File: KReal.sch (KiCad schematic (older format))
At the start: 30 parts, among them J101 USB, J102 3mm, J103 3mm, J104 3mm, J105 3mm, P101 X AXIS, P102 Y AXIS, P103 Z AXIS, P104 A AXIS, P105 X SW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

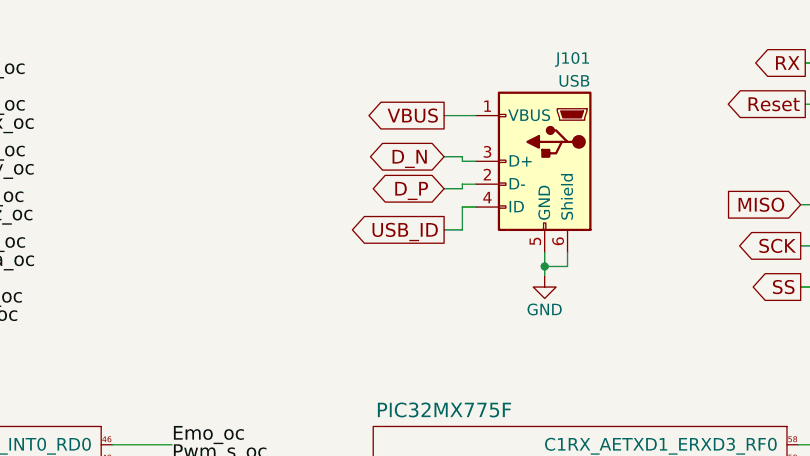
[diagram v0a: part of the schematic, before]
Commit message: Fixed swapped USB N and P lanes in schematic. NOT fixed in layout yet.
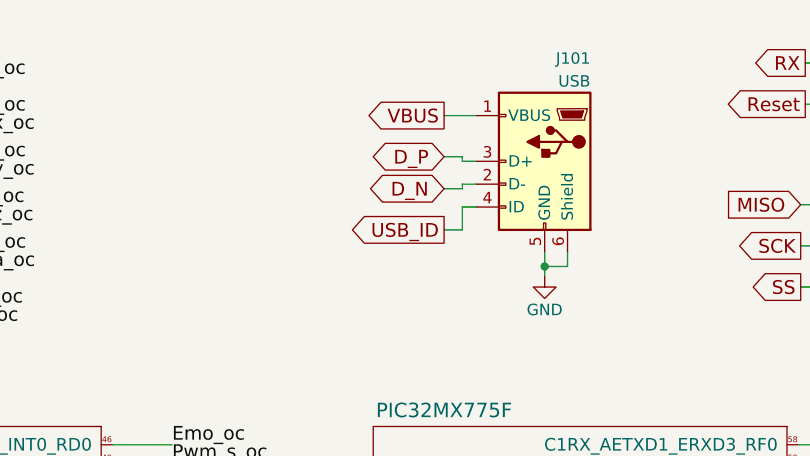
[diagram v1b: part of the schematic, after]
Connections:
- net D_N: now also J101.2 (D-); no longer J101.3 (D+)
- net D_P: now also J101.3 (D+); no longer J101.2 (D-)
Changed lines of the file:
@@
 VBUS
 Text GLabel 8620 1180 0    60   BiDi ~ 0
+D_P
+Text GLabel 8620 1320 0    60   BiDi ~ 0
 D_N
-Text GLabel 8620 1320 0    60   BiDi ~ 0
-D_P
 Text GLabel 8620 1500 0    60   Output ~ 0
 USB_ID

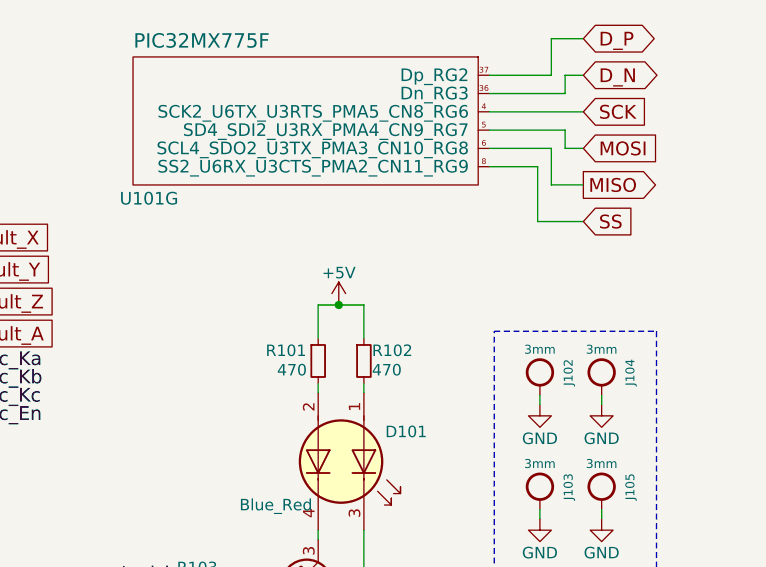
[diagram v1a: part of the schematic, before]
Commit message: Fixed USB in layout. Fixed LEDs power source.
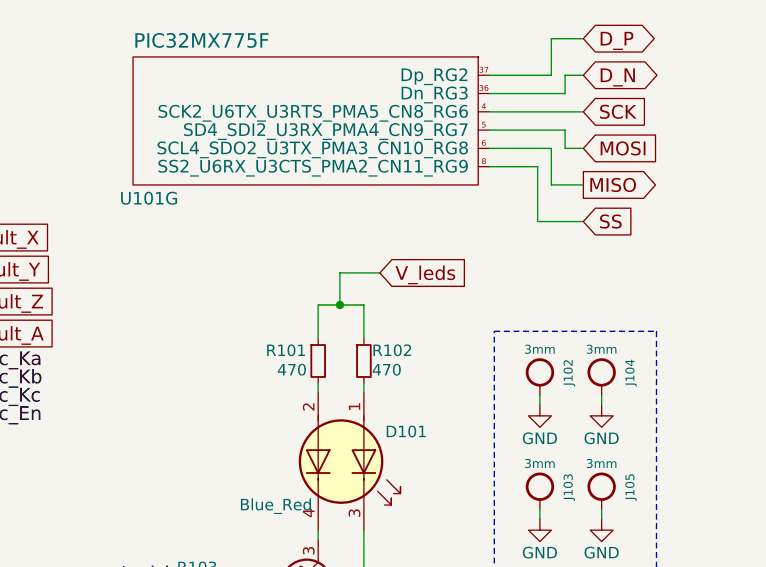
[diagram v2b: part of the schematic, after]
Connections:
- net +5V: no longer R101.1, R102.1
- new net V_leds: R101.1, R102.1
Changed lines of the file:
@@
 Title "KReal"
 Date ""
-Rev "0.2"
+Rev "0.5"
 Comp "TiZed"
 Comment1 ""
@@
 	9420 5270 9420 5310
 $Comp
-L +5V #PWR033
-U 1 1 5907D354
-P 9510 4285
-F 0 "#PWR033" H 9510 4135 50  0001 C CNN
-F 1 "+5V" H 9510 4425 50  0000 C CNN
-F 2 "" H 9510 4285 50  0001 C CNN
-F 3 "" H 9510 4285 50  0001 C CNN
-	1    9510 4285
-	1    0    0    -1
-$EndComp
-$Comp
 L Q_NPN_BEC Q101
 U 1 1 5907D80E
@@
 Wire Wire Line
 	9420 4285 9620 4285
-Connection ~ 9510 4285
+Text GLabel 9690 4145 2    60   Input ~ 0
+V_leds
+Wire Wire Line
+	9515 4145 9690 4145
+Wire Wire Line
+	9515 4145 9515 4285
+Connection ~ 9515 4285
 $EndSCHEMATC
